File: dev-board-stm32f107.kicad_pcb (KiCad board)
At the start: 2 copper layers, 4 parts, among them U100 LT8609

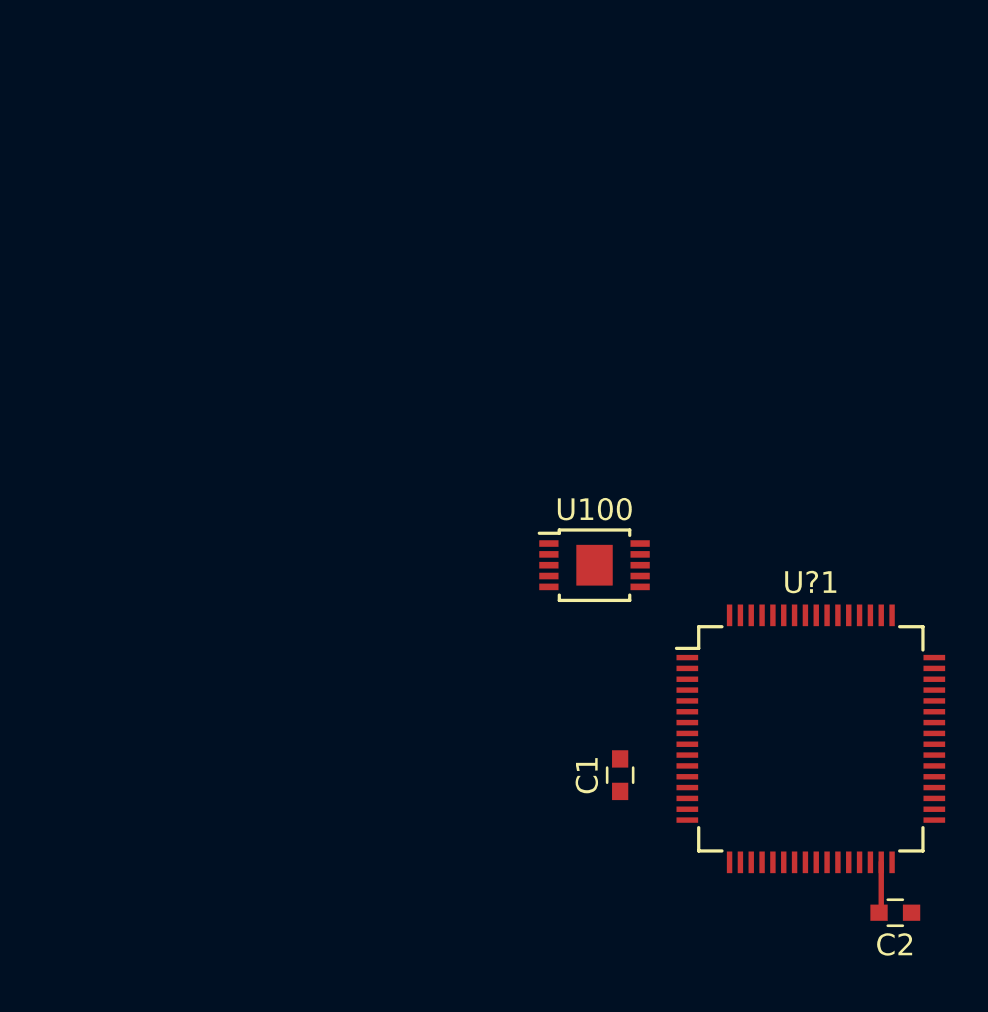
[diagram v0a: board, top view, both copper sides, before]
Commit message: added footprints for power components. Updated netlist.
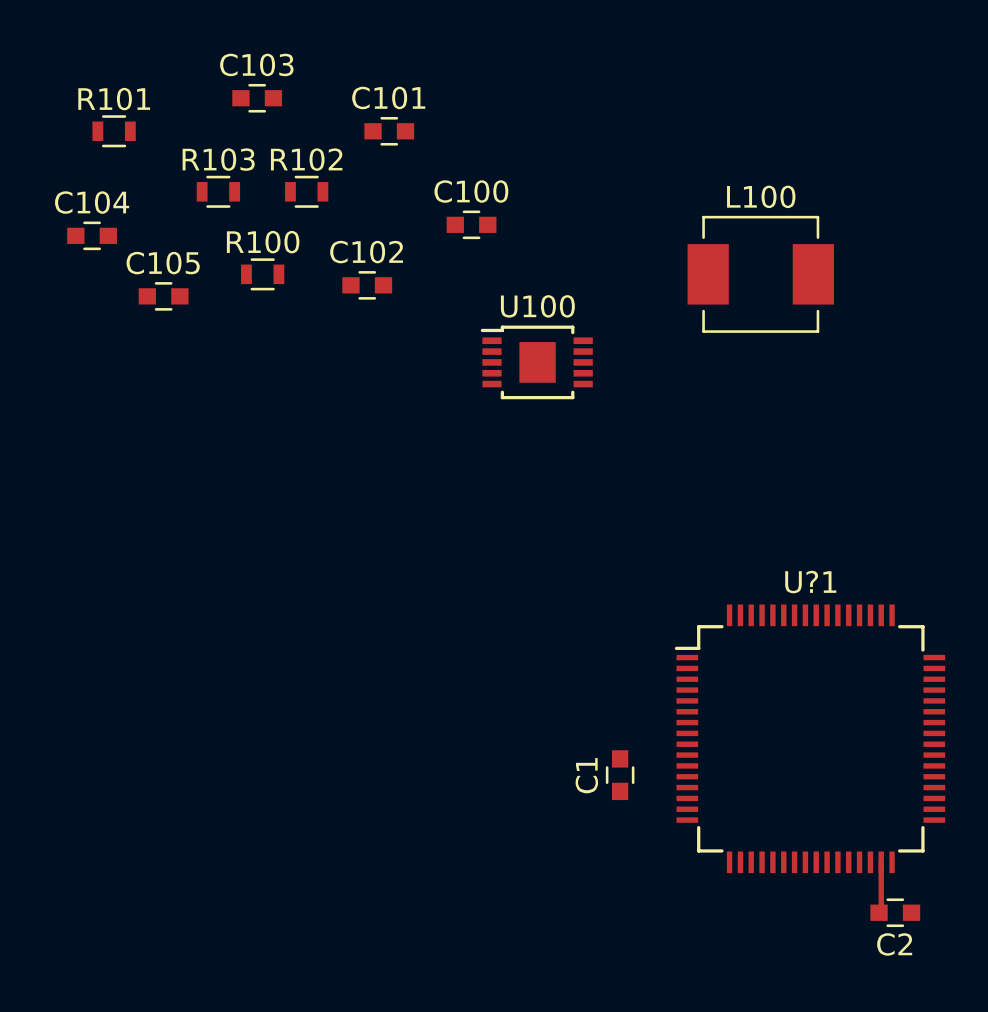
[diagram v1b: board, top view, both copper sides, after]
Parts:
- added C100: 4.7uF, Capacitors_SMD:C_0603, F.Cu at (132.8, 81.3)
- added C101: 1uF, Capacitors_SMD:C_0603, F.Cu at (129.0, 77.0)
- added C102: 10nF, Capacitors_SMD:C_0603, F.Cu at (128.0, 84.1)
- added C103: 0.1uF, Capacitors_SMD:C_0603, F.Cu at (122.9, 75.4)
- added C104: 10pF, Capacitors_SMD:C_0603, F.Cu at (115.3, 81.8)
- added C105: 22uF, Capacitors_SMD:C_0603, F.Cu at (118.6, 84.6)
- added L100: 2.2uH, Inductors_SMD:L_Vishay_IHLP-2020, F.Cu at (146.2, 83.6)
- added R100: 18.2k, Resistors_SMD:R_0603, F.Cu at (123.2, 83.6)
- added R101: 100k, Resistors_SMD:R_0603, F.Cu at (116.3, 77.0)
- added R102: 309k, Resistors_SMD:R_0603, F.Cu at (125.2, 79.8)
- added R103: 1M, Resistors_SMD:R_0603, F.Cu at (121.2, 79.8)
- moved U100 9.72 mm to (135.9, 87.6)
